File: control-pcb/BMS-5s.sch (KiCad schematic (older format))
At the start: 9 parts, among them P1 Conn_Switch-N-Sense, P2 CONN_01X06

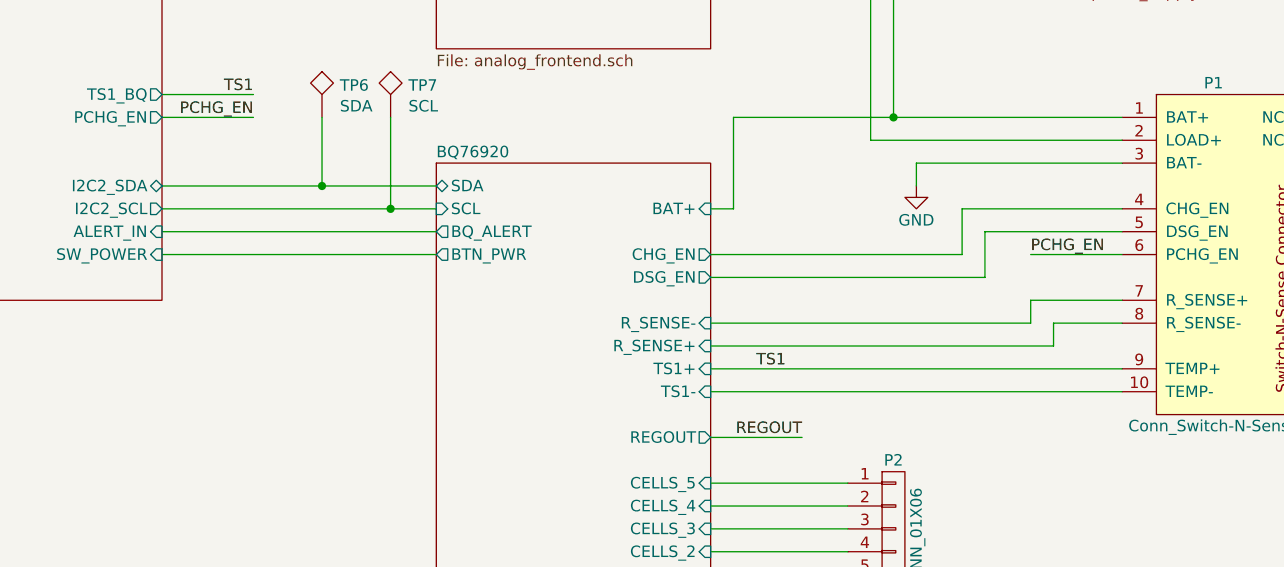
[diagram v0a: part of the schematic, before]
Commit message: Issues #1, #2 and #4 fixed
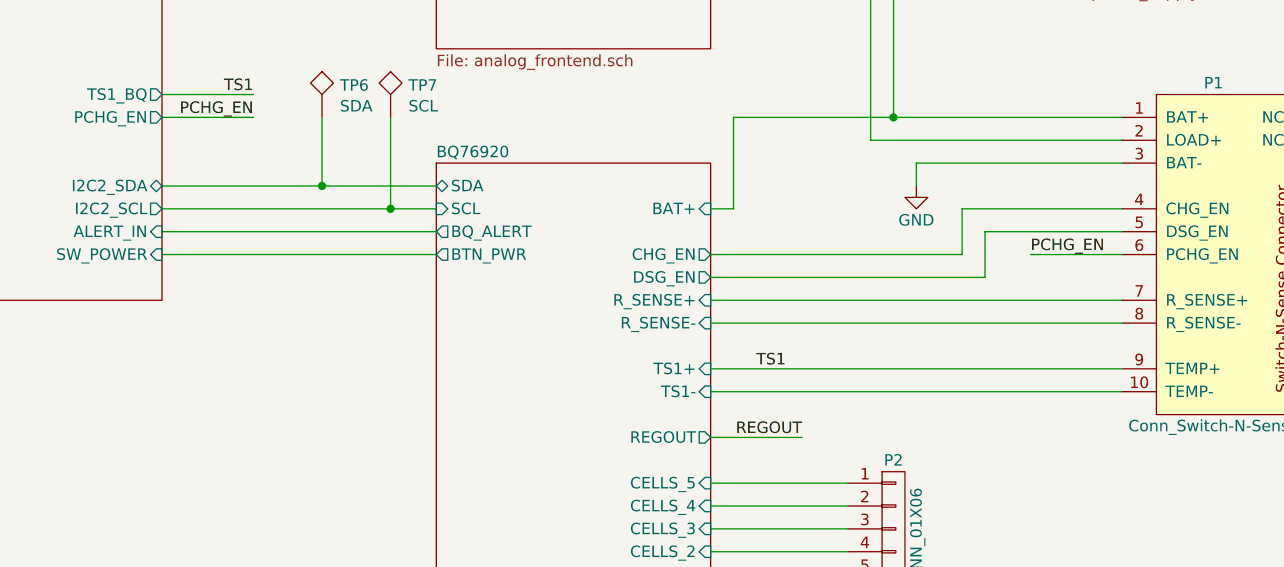
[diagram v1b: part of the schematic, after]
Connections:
- net BQ76920/R_SENSE+: now also P1.7 (R_SENSE+); no longer P1.8 (R_SENSE-)
- net BQ76920/R_SENSE-: now also P1.8 (R_SENSE-); no longer P1.7 (R_SENSE+)
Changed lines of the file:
@@
 EESchema Schematic File Version 2
-LIBS:BMS-5s-rescue
 LIBS:IEC-60617
 LIBS:LibreSolar
@@
 F14 "BAT+" I R 7400 3500 50
 F15 "R_SENSE-" I R 7400 4000 50
-F16 "R_SENSE+" I R 7400 4100 50
+F16 "R_SENSE+" I R 7400 3900 50
 F17 "TS1+" I R 7400 4200 50
 F18 "TS1-" I R 7400 4300 50
@@
 	8600 3800 7400 3800
 Wire Wire Line
-	7400 4000 8800 4000
-Wire Wire Line
-	8800 4000 8800 3900
-Wire Wire Line
-	8800 3900 9200 3900
-Wire Wire Line
-	7400 4100 8900 4100
-Wire Wire Line
-	8900 4100 8900 4000
-Wire Wire Line
-	8900 4000 9200 4000
+	7400 3900 9200 3900
 Wire Wire Line
 	7400 4200 9200 4200
@@
 	5000 3400 6200 3400
 Wire Wire Line
-	6200 3500 5000 3500
+	5000 3500 6200 3500
 Wire Wire Line
 	5000 3600 6200 3600
@@
 	6000 3100 6000 3500
 Connection ~ 6000 3500
+Wire Wire Line
+	7400 4000 9200 4000
 $EndSCHEMATC

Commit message: Update to KiCAD 5 and minor changes in part selection
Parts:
- LOGO1: value OPEN_HARDWARE_1 -> OPEN_HARDWARE; footprint Symbols:OSHW-Logo_5.7x6mm_SilkScreen -> Symbol:OSHW-Logo_5.7x6mm_SilkScreen; symbol OPEN_HARDWARE_1 -> Project:Logo_Open_Hardware_Small
- LOGO2: symbol LIBRE_SOLAR -> Project:LibreSolar_Logo
- P1: symbol Conn_Switch-N-Sense -> Project:Conn_Switch-N-Sense
- P2: symbol CONN_01X06 -> Project:Conn_01x06
- TP3, TP4, TP5, TP6, TP7: symbol TEST -> Connector:Test_Point
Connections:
- wire segments 57 -> 64
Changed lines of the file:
@@
-EESchema Schematic File Version 2
-LIBS:IEC-60617
-LIBS:LibreSolar
-LIBS:power
-LIBS:device
-LIBS:conn
-LIBS:logo
+EESchema Schematic File Version 4
 LIBS:BMS-5s-cache
 EELAYER 26 0
@@
 Sheet 1 6
 Title "Libre Solar BMS 5s"
-Date "2017-05-27"
-Rev "0.1"
+Date "2018-05-11"
+Rev "0.2"
 Comp "Libre Solar (http://libre.solar)"
 Comment1 "License: CC-BY-SA"
@@
 $EndSheet
 $Comp
-L Conn_Switch-N-Sense P1
+L Project:Conn_Switch-N-Sense P1
 U 1 1 58E8147B
 P 9600 3700
@@
 $EndSheet
 $Comp
-L CONN_01X06 P2
+L Project:Conn_01x06 P2
 U 1 1 58F30336
-P 8200 4950
-F 0 "P2" H 8200 5300 50  0000 C CNN
-F 1 "CONN_01X06" V 8300 4950 50  0000 C CNN
-F 2 "LibreSolar:Phoenix_Contact_MC_1,5_6-G-3,81" H 8200 4950 50  0001 C CNN
-F 3 "" H 8200 4950 50  0000 C CNN
-F 4 "Phoenix Contact" H 8200 4950 60  0001 C CNN "Manufacturer"
-F 5 "1803316" H 8200 4950 60  0001 C CNN "PartNumber"
-F 6 "MC 1,5/ 6-G-3,81" H 8200 4950 60  0001 C CNN "Remarks"
-	1    8200 4950
+P 8200 4900
+F 0 "P2" H 8200 5250 50  0000 C CNN
+F 1 "CONN_01X06" V 8300 4900 50  0000 C CNN
+F 2 "LibreSolar:Phoenix_Contact_MC_1,5_6-G-3,81" H 8200 4900 50  0001 C CNN
+F 3 "" H 8200 4900 50  0000 C CNN
+F 4 "Phoenix Contact" H 8200 4900 60  0001 C CNN "Manufacturer"
+F 5 "1803316" H 8200 4900 60  0001 C CNN "PartNumber"
+F 6 "MC 1,5/ 6-G-3,81" H 8200 4900 60  0001 C CNN "Remarks"
+	1    8200 4900
 	1    0    0    -1
 $EndComp
@@
 	7400 4300 9200 4300
 Wire Wire Line
-	7400 2100 8900 2100
-Wire Wire Line
-	7500 3100 9200 3100
+	7400 2100 8000 2100
+Wire Wire Line
+	7500 3100 8200 3100
 Wire Wire Line
 	8200 3100 8200 2100
@@
 Connection ~ 8200 3100
 Wire Wire Line
-	7400 2200 8100 2200
+	7400 2200 7600 2200
 Wire Wire Line
 	8100 2200 8100 3200
@@
 	8100 3200 9200 3200
 $Comp
-L GND #PWR01
+L power:GND #PWR01
 U 1 1 58F56B2A
 P 8300 3400
@@
 PCHG_EN
 Wire Wire Line
-	5000 3400 6200 3400
-Wire Wire Line
-	5000 3500 6200 3500
+	5000 3400 5700 3400
+Wire Wire Line
+	5000 3500 6000 3500
 Wire Wire Line
 	5000 3600 6200 3600
@@
 REGOUT
 Wire Wire Line
-	8300 2300 8900 2300
+	8300 2300 8700 2300
 Text Label 8300 2300 0    50   ~ 0
 REGOUT
@@
 	2700 3700 3600 3700
 $Comp
-L LIBRE_SOLAR LOGO2
+L Project:LibreSolar_Logo LOGO2
 U 1 1 58F7CBC4
 P 5650 7050
@@
 $EndComp
 $Comp
-L OPEN_HARDWARE_1 LOGO1
+L Project:Logo_Open_Hardware_Small LOGO1
 U 1 1 58F7CD5F
 P 4900 7050
 F 0 "LOGO1" H 4900 7325 50  0000 C CNN
-F 1 "OPEN_HARDWARE_1" H 4900 6825 50  0000 C CNN
-F 2 "Symbols:OSHW-Logo_5.7x6mm_SilkScreen" H 4900 7050 50  0001 C CNN
+F 1 "OPEN_HARDWARE" H 4900 6825 50  0000 C CNN
+F 2 "Symbol:OSHW-Logo_5.7x6mm_SilkScreen" H 4900 7050 50  0001 C CNN
 F 3 "" H 4900 7050 50  0001 C CNN
 	1    4900 7050
@@
 	6200 3700 5000 3700
 $Comp
-L TEST TP4
+L Connector:Test_Point TP4
 U 1 1 591748EB
 P 8000 1700
@@
 Connection ~ 8000 2100
 $Comp
-L TEST TP5
+L Connector:Test_Point TP5
 U 1 1 591783E5
 P 8700 1700
@@
 $EndComp
 $Comp
-L TEST TP3
+L Connector:Test_Point TP3
 U 1 1 5917857D
 P 7600 1700
@@
 Connection ~ 8700 2300
 $Comp
-L TEST TP6
+L Connector:Test_Point TP6
 U 1 1 5917D3E9
 P 5700 3100
@@
 $EndComp
 $Comp
-L TEST TP7
+L Connector:Test_Point TP7
 U 1 1 5917D5BB
 P 6000 3100
@@
 Wire Wire Line
 	7400 4000 9200 4000
+Wire Wire Line
+	8200 2100 8900 2100
+Wire Wire Line
+	8200 3100 9200 3100
+Wire Wire Line
+	8000 2100 8200 2100
+Wire Wire Line
+	7600 2200 8100 2200
+Wire Wire Line
+	8700 2300 8900 2300
+Wire Wire Line
+	5700 3400 6200 3400
+Wire Wire Line
+	6000 3500 6200 3500
 $EndSCHEMATC
